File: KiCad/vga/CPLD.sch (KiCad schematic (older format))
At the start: 27 parts, among them U1 EPM7128S, U14 EPM7064S, X1 50 MHz

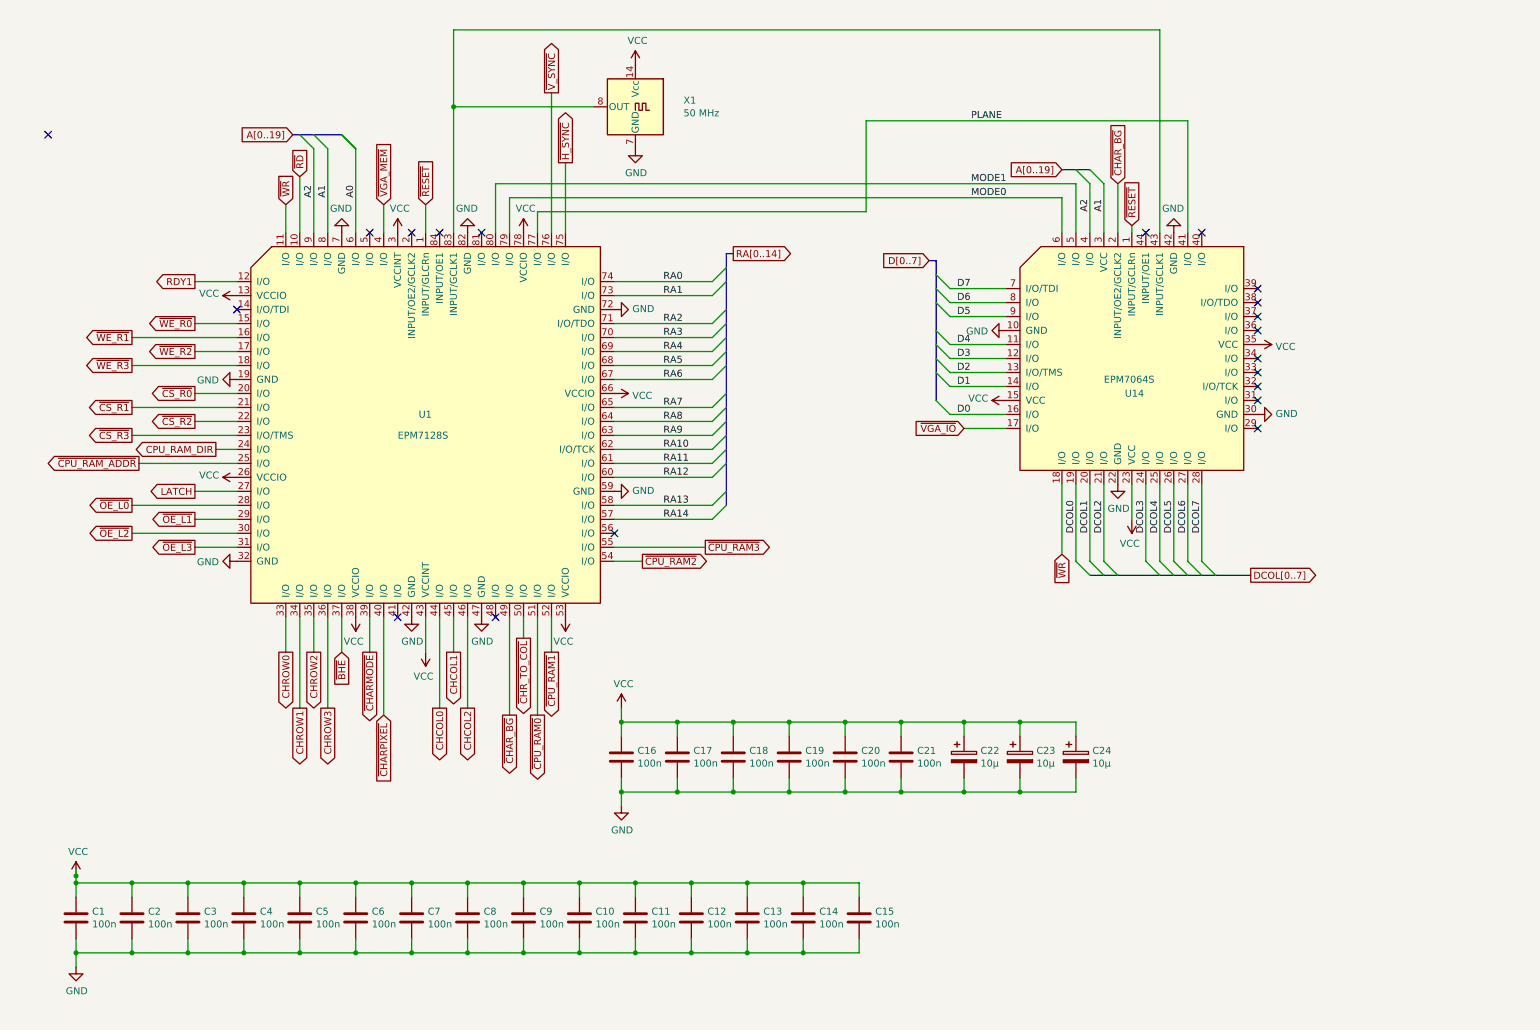
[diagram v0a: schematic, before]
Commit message: Updated graphics adapter and main schematics + board.
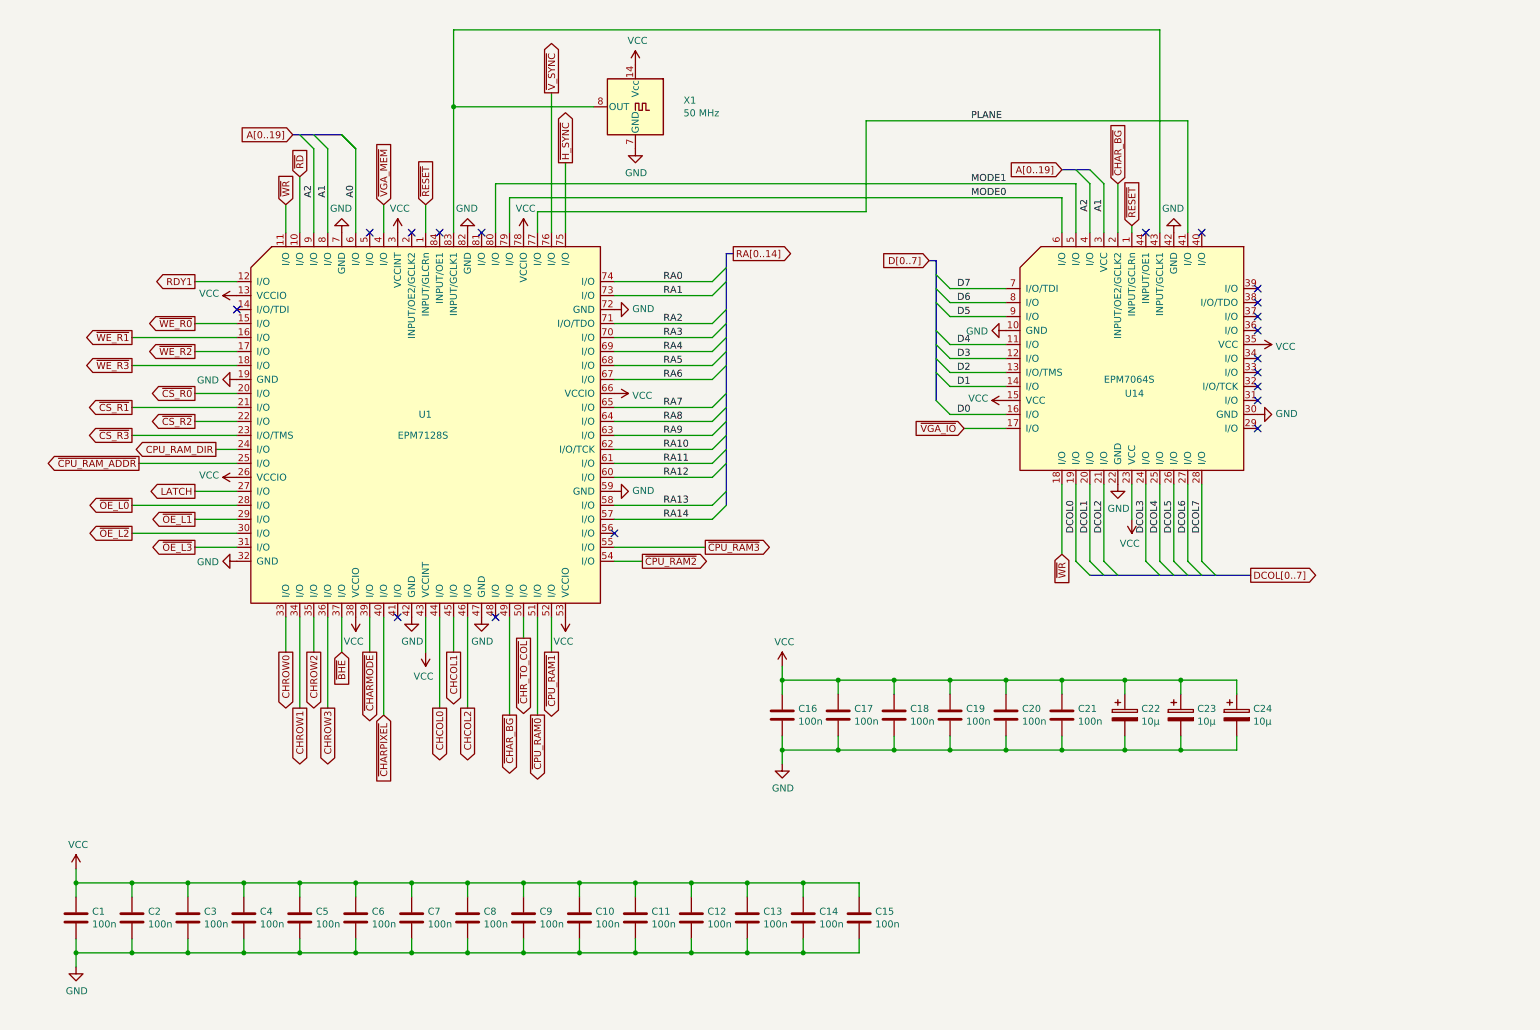
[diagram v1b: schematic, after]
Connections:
- no-connect marks 20 -> 19
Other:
- moved on the sheet: C16, C17, C18, C19, C20, C21, C22, C23, C24

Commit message: Updated KiCad VGA board and main board.
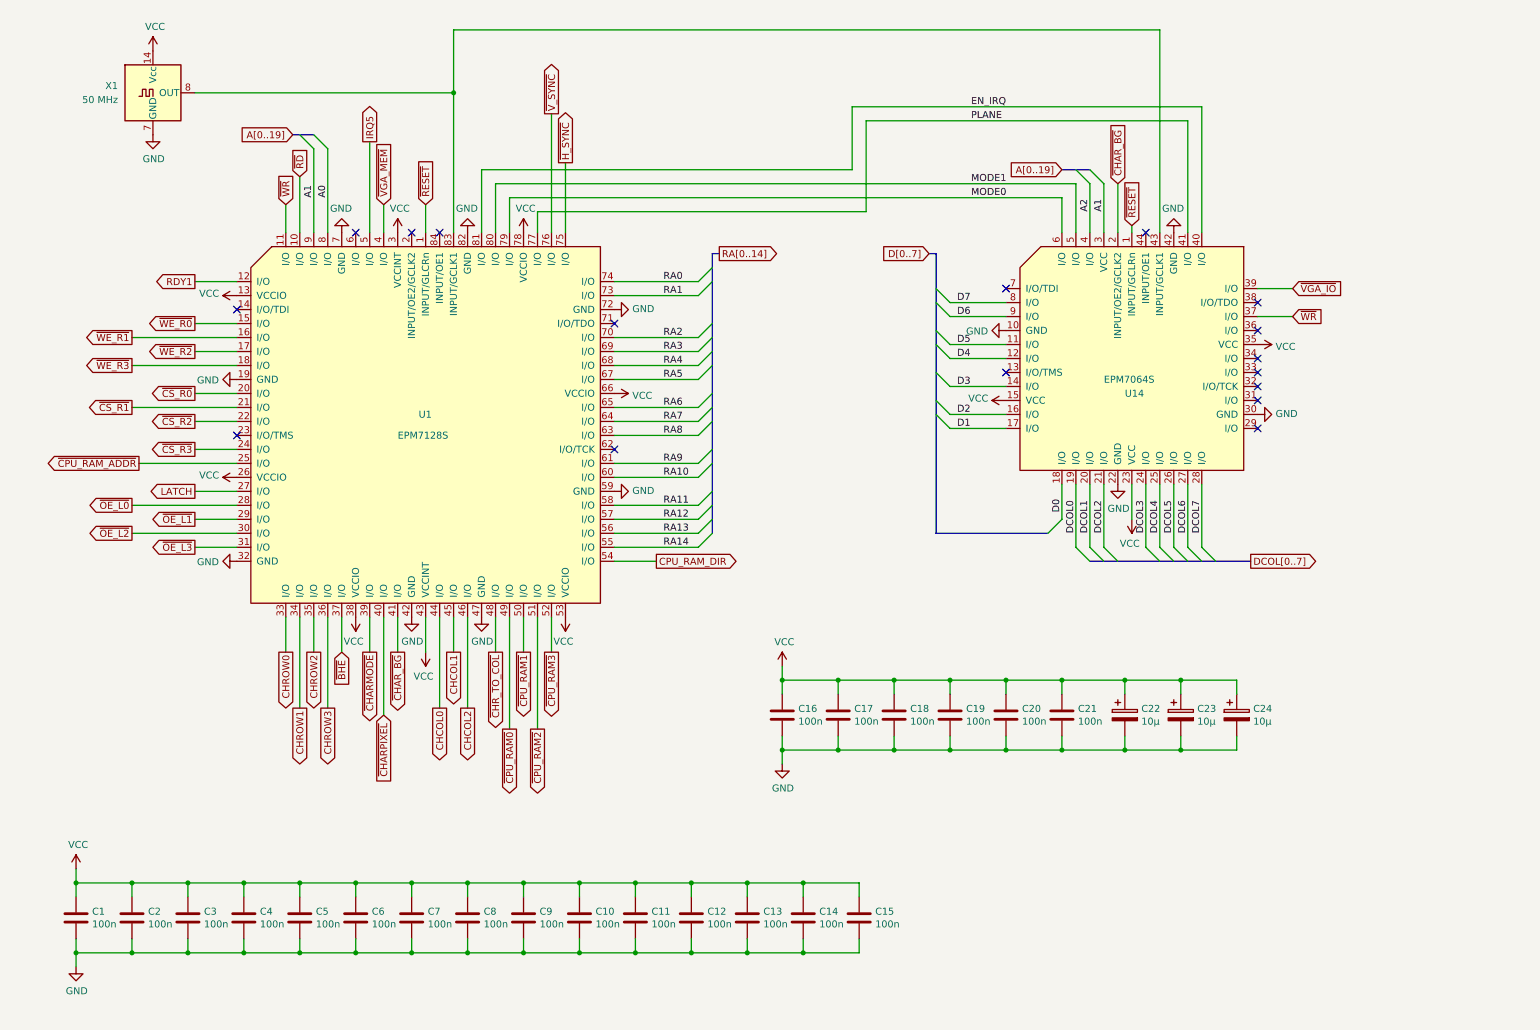
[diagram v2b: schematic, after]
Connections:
- net A0: now also U1.8 (I/O); no longer U1.6 (I/O)
- net A1: now also U1.9 (I/O); no longer U1.8 (I/O)
- net A2: no longer U1.9 (I/O)
- net CPU_RAM_DIR: now also U1.54 (I/O); no longer U1.24 (I/O)
- net D0: now also U14.18 (I/O); no longer U14.16 (I/O)
- net D1: now also U14.17 (I/O); no longer U14.14 (I/O)
- net D2: now also U14.16 (I/O); no longer U14.13 (I/O/TMS)
- net D3: now also U14.14 (I/O); no longer U14.12 (I/O)
- net D4: now also U14.12 (I/O); no longer U14.11 (I/O)
- net D5: now also U14.11 (I/O); no longer U14.9 (I/O)
- net D6: now also U14.9 (I/O); no longer U14.8 (I/O)
- net D7: now also U14.8 (I/O); no longer U14.7 (I/O/TDI)
- net RA10: now also U1.60 (I/O); no longer U1.62 (I/O/TCK)
- net RA11: now also U1.58 (I/O); no longer U1.61 (I/O)
- net RA12: now also U1.57 (I/O); no longer U1.60 (I/O)
- net RA13: now also U1.56 (I/O); no longer U1.58 (I/O)
- net RA14: now also U1.55 (I/O); no longer U1.57 (I/O)
- net RA2: now also U1.70 (I/O); no longer U1.71 (I/O/TDO)
- net RA3: now also U1.69 (I/O); no longer U1.70 (I/O)
- net RA4: now also U1.68 (I/O); no longer U1.69 (I/O)
- net RA5: now also U1.67 (I/O); no longer U1.68 (I/O)
- net RA6: now also U1.65 (I/O); no longer U1.67 (I/O)
- net RA7: now also U1.64 (I/O); no longer U1.65 (I/O)
- net RA8: now also U1.63 (I/O); no longer U1.64 (I/O)
- net RA9: now also U1.61 (I/O); no longer U1.63 (I/O)
- net ~CHAR_BG: now also U1.41 (I/O); no longer U1.49 (I/O)
- net ~CHR_TO_COL: now also U1.48 (I/O); no longer U1.50 (I/O)
- net ~CPU_RAM0: now also U1.49 (I/O); no longer U1.51 (I/O)
- net ~CPU_RAM1: now also U1.50 (I/O); no longer U1.52 (I/O)
- net ~CPU_RAM2: now also U1.51 (I/O); no longer U1.54 (I/O)
- net ~CPU_RAM3: now also U1.52 (I/O); no longer U1.55 (I/O)
- net ~CS_R3: now also U1.24 (I/O); no longer U1.23 (I/O/TMS)
- net ~VGA_IO: now also U14.39 (I/O); no longer U14.17 (I/O)
- net ~WR: now also U14.37 (I/O); no longer U14.18 (I/O)
- net IRQ5: now reaches U1.5 (I/O)
- net EN_IRQ: now reaches U1.81 (I/O)
- net EN_IRQ: now also U14.40 (I/O)
- no-connect marks 19 -> 17
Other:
- moved on the sheet: X1

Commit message: Updated graphics adapter
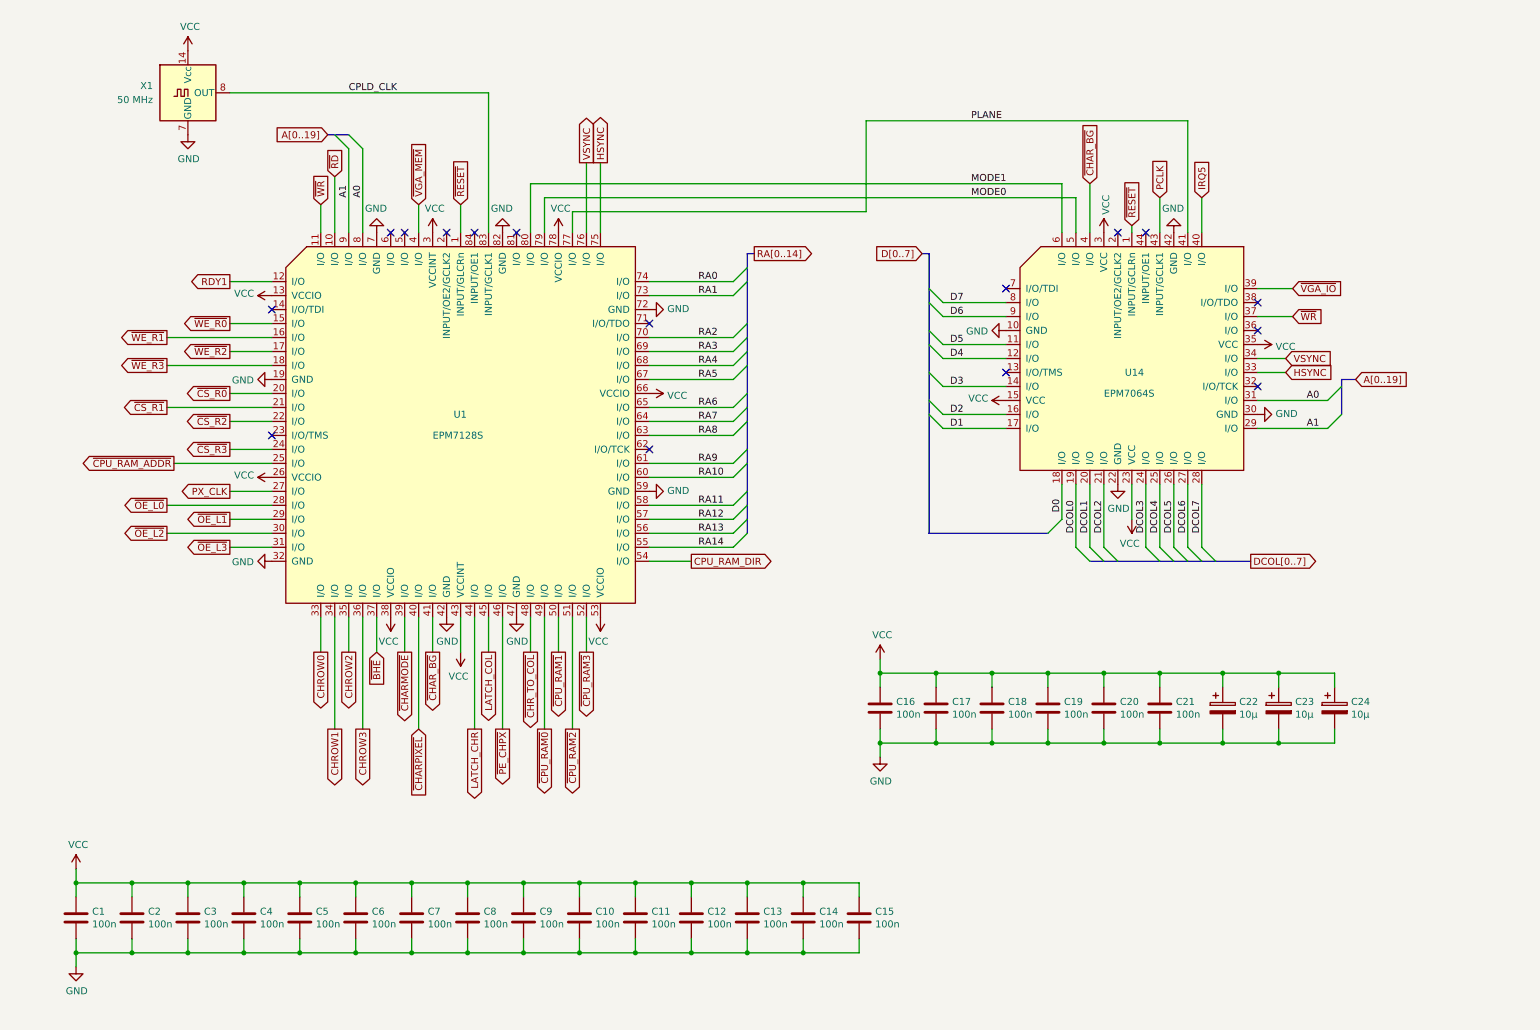
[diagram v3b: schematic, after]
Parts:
- C17: footprint Capacitor_THT:C_Disc_D3.4mm_W2.1mm_P2.50mm -> Capacitor_THT:C_Disc_D4.3mm_W1.9mm_P5.00mm
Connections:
- net A2 is gone; now on net ~CHAR_BG: U14.4 (I/O)
- net ~H_SYNC is gone; now on net HSYNC: U1.75 (I/O)
- net ~V_SYNC is gone; now on net VSYNC: U1.76 (I/O)
- net A0: now also U14.31 (I/O)
- net A1: now also U14.29 (I/O); no longer U14.3 (VCC)
- net IRQ5: now also U14.40 (I/O); no longer U1.5 (I/O)
- net MODE0: now also U14.5 (I/O); no longer U14.6 (I/O)
- net MODE1: now also U14.6 (I/O); no longer U14.5 (I/O)
- net VCC: now also U14.3 (VCC)
- net ~CHAR_BG: no longer U14.2 (INPUT/OE2/GCLK2)
- net CPLD_CLK: now reaches U1.83 (INPUT/GCLK1), X1.8 (OUT)
- net CPLD_CLK: no longer U14.43 (INPUT/GCLK1)
- net HSYNC: now reaches U14.33 (I/O)
- net VSYNC: now reaches U14.34 (I/O)
- net CHCOL0 renamed LATCH_CHR
- net CHCOL1 renamed LATCH_COL
- net CHCOL2 renamed ~PE_CHPX
- net EN_IRQ: no longer names the net of U1.81 (I/O)
- net EN_IRQ: no longer U14.40 (I/O)
- net LATCH renamed PX_CLK
- new net PCLK: U14.43 (INPUT/GCLK1)
- no-connect marks 17 -> 16
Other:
- moved on the sheet: C16, C17, C18, C19, C20, C21, C22, C23, C24, U1, X1
